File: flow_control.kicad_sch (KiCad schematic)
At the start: 64 parts, among them J10 Pump 1, J11 Temperature, J12 Pump 2, J13 Pump 3, J3 Flow, J7 Valve 1, J8 Valve 2, J9 Valve 3, Q1 MMBT3904, Q10 AO3401A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

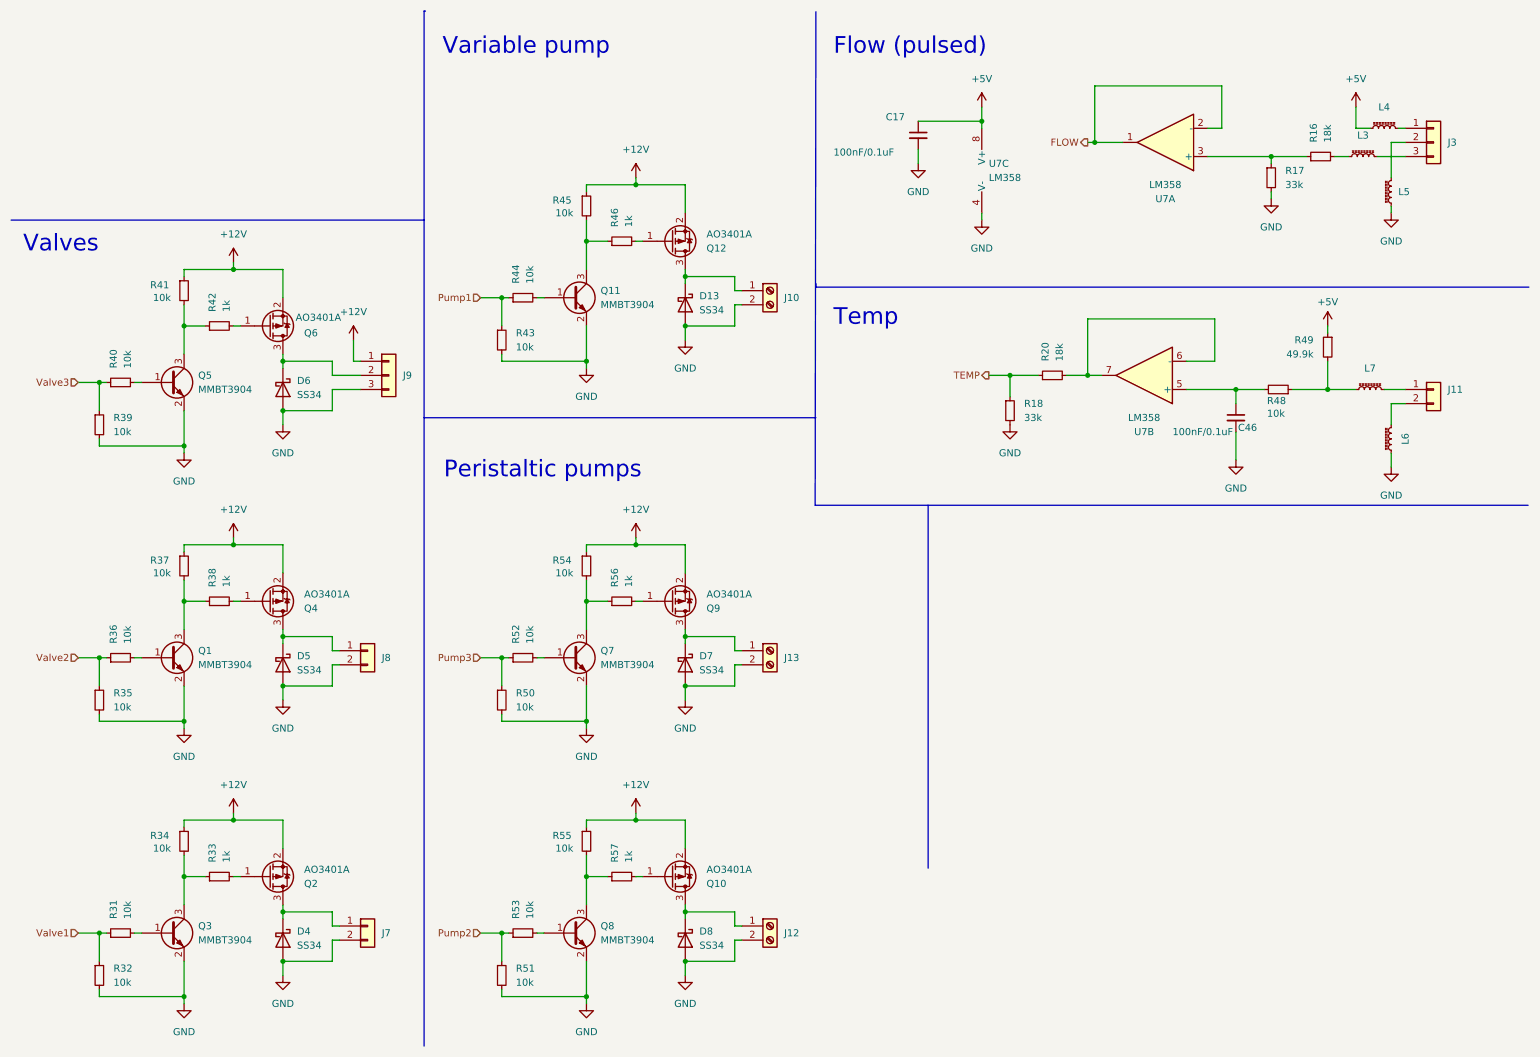
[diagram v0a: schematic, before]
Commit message: Replace 4 of the 6 highside outputs with TPS4H160B
See #50
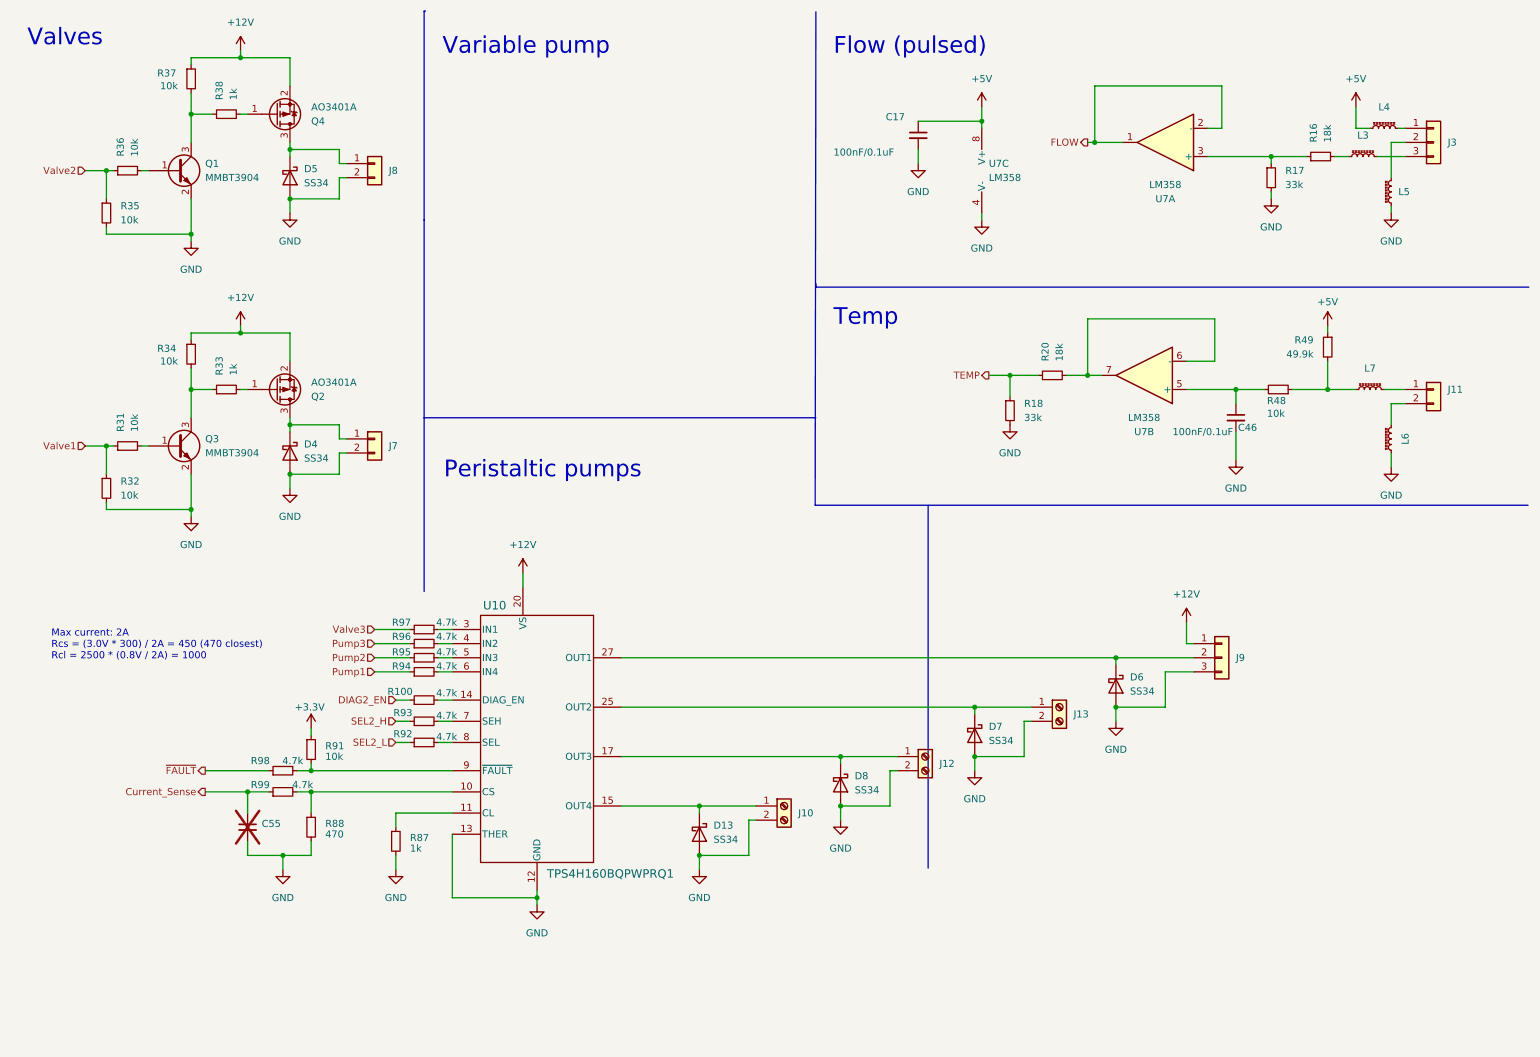
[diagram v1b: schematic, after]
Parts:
- removed Q10, Q12, Q6, Q9: AO3401A, Package_TO_SOT_SMD:SOT-23, symbol Transistor_FET:AO3401A
- removed Q11, Q5, Q7, Q8: MMBT3904, Package_TO_SOT_SMD:SOT-23, symbol Transistor_BJT:MMBT3904
- removed R39, R40, R41, R43, R44, R45, R50, R51, R52, R53, R54, R55: 10k, Resistor_SMD:R_0603_1608Metric, symbol Device:R_Small
- removed R42, R46, R56, R57: 1k, Resistor_SMD:R_0603_1608Metric, symbol Device:R_Small
- added C55: ~, Capacitor_SMD:C_0402_1005Metric, symbol Device:C_Small
- added R100, R92, R93, R94, R95, R96, R97, R98, R99: 4.7k, Resistor_SMD:R_0402_1005Metric, symbol Device:R_Small
- added R87: 1k, Resistor_SMD:R_0402_1005Metric, symbol Device:R_Small
- added R88: 470, Resistor_SMD:R_0402_1005Metric, symbol Device:R_Small
- added R91: 10k, Resistor_SMD:R_0402_1005Metric, symbol Device:R_Small
- added U10: TPS4H160BQPWPRQ1, Package_SO:HTSSOP-28-1EP_4.4x9.7mm_P0.65mm_EP2.85x5.4mm_ThermalVias, symbol HydroponicFlowerControl:TPS4H160BQPWPRQ1
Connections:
- net +12V: now also U10.20 (VS), U10.21 (VS), U10.22 (VS), U10.23 (VS)
- net GND: now also C55.2, R87.2, R88.2, U10.1 (GND), U10.12 (GND), U10.13 (THER), U10.29 (PAD)
- net Pump1: now also R94.1
- net Pump2: now also R95.1
- net Pump3: now also R96.1
- net Valve3: now also R97.1
- net at D7.1 (K), J13.1 (Pin_1): now also U10.25 (OUT2), U10.26 (OUT2)
- net at D8.1 (K), J12.1 (Pin_1): now also U10.17 (OUT3), U10.18 (OUT3)
- net at D13.1 (K), J10.1 (Pin_1): now also U10.15 (OUT4), U10.16 (OUT4)
- net at D6.1 (K), J9.2 (Pin_2): now also U10.27 (OUT1), U10.28 (OUT1)
- new net: R92.2, U10.8 (SEL)
- new net: R88.1, R99.2, U10.10 (CS)
- new net: R87.1, U10.11 (CL)
- new net: R100.2, U10.14 (DIAG_EN)
- new net: R97.2, U10.3 (IN1)
- new net: R96.2, U10.4 (IN2)
- new net: R95.2, U10.5 (IN3)
- new net: R94.2, U10.6 (IN4)
- new net: R93.2, U10.7 (SEH)
- new net: R91.2, R98.2, U10.9 (~{FAULT})
- new net +3.3V: R91.1
- new net Current_Sense: C55.1, R99.1
- new net DIAG2_EN: R100.1
- new net SEL2_H: R93.1
- new net SEL2_L: R92.1
- new net ~{FAULT}: R98.1
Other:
- note added: "Max current: 2A Rcs = (3.0V * 300) / 2A = 450 (470 closest) Rcl = 2500 * (0.8V / 2A) = 1000"
- moved on the sheet: D13, D4, D5, D6, D7, D8, J10, J12, J13, J7, J8, J9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

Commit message: Replace the last 2 of the highside outputs with TPS4H160B
Closes #50
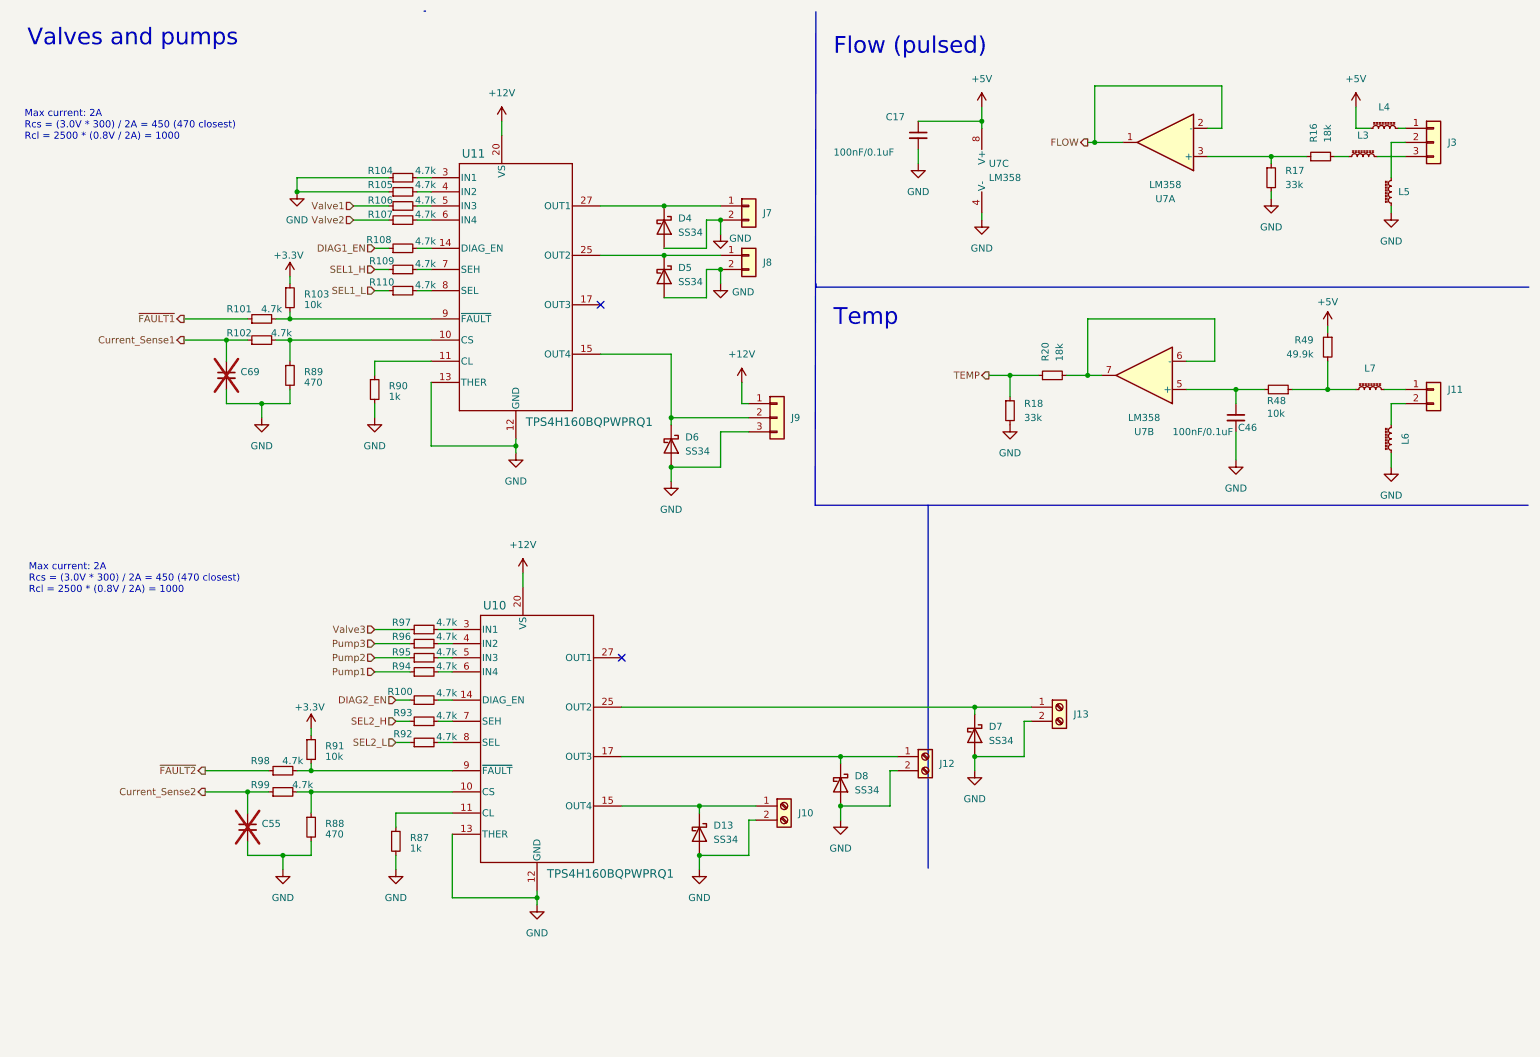
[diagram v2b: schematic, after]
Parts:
- removed Q1, Q3: MMBT3904, Package_TO_SOT_SMD:SOT-23, symbol Transistor_BJT:MMBT3904
- removed Q2, Q4: AO3401A, Package_TO_SOT_SMD:SOT-23, symbol Transistor_FET:AO3401A
- removed R31, R32, R34, R35, R36, R37: 10k, Resistor_SMD:R_0603_1608Metric, symbol Device:R_Small
- removed R33, R38: 1k, Resistor_SMD:R_0603_1608Metric, symbol Device:R_Small
- added C69: ~, Capacitor_SMD:C_0402_1005Metric, symbol Device:C_Small
- added R101, R102, R104, R105, R106, R107, R108, R109, R110: 4.7k, Resistor_SMD:R_0402_1005Metric, symbol Device:R_Small
- added R103: 10k, Resistor_SMD:R_0402_1005Metric, symbol Device:R_Small
- added R89: 470, Resistor_SMD:R_0402_1005Metric, symbol Device:R_Small
- added R90: 1k, Resistor_SMD:R_0402_1005Metric, symbol Device:R_Small
- added U11: TPS4H160BQPWPRQ1, Package_SO:HTSSOP-28-1EP_4.4x9.7mm_P0.65mm_EP2.85x5.4mm_ThermalVias, symbol HydroponicFlowerControl:TPS4H160BQPWPRQ1
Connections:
- net +12V: now also U11.20 (VS), U11.21 (VS), U11.22 (VS), U11.23 (VS)
- net +3.3V: now also R103.1
- net GND: now also C69.2, R104.1, R105.1, R89.2, R90.2, U11.1 (GND), U11.12 (GND), U11.13 (THER), U11.29 (PAD)
- net Valve1: now also R106.1
- net Valve2: now also R107.1
- net at D4.1 (K), J7.1 (Pin_1): now also U11.27 (OUT1), U11.28 (OUT1)
- net at D5.1 (K), J8.1 (Pin_1): now also U11.25 (OUT2), U11.26 (OUT2)
- net at D6.1 (K), J9.2 (Pin_2): now also U11.15 (OUT4), U11.16 (OUT4); no longer U10.27 (OUT1), U10.28 (OUT1)
- net Current_Sense renamed Current_Sense2
- net ~{FAULT} renamed ~{FAULT2}
- new net: R102.2, R89.1, U11.10 (CS)
- new net: R90.1, U11.11 (CL)
- new net: R108.2, U11.14 (DIAG_EN)
- new net: U11.17 (OUT3), U11.18 (OUT3)
- new net: R104.2, U11.3 (IN1)
- new net: R105.2, U11.4 (IN2)
- new net: R106.2, U11.5 (IN3)
- new net: R107.2, U11.6 (IN4)
- new net: R109.2, U11.7 (SEH)
- new net: R110.2, U11.8 (SEL)
- new net: R101.2, R103.2, U11.9 (~{FAULT})
- new net: U10.27 (OUT1), U10.28 (OUT1)
- new net Current_Sense1: C69.1, R102.1
- new net DIAG1_EN: R108.1
- new net SEL1_H: R109.1
- new net SEL1_L: R110.1
- new net ~{FAULT1}: R101.1
- no-connect marks 0 -> 2
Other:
- note added: "Valves and pumps"
- note removed: "Peristaltic pumps"
- note removed: "Valves"
- note removed: "Variable pump"
- moved on the sheet: D4, D5, D6, J7, J8, J9

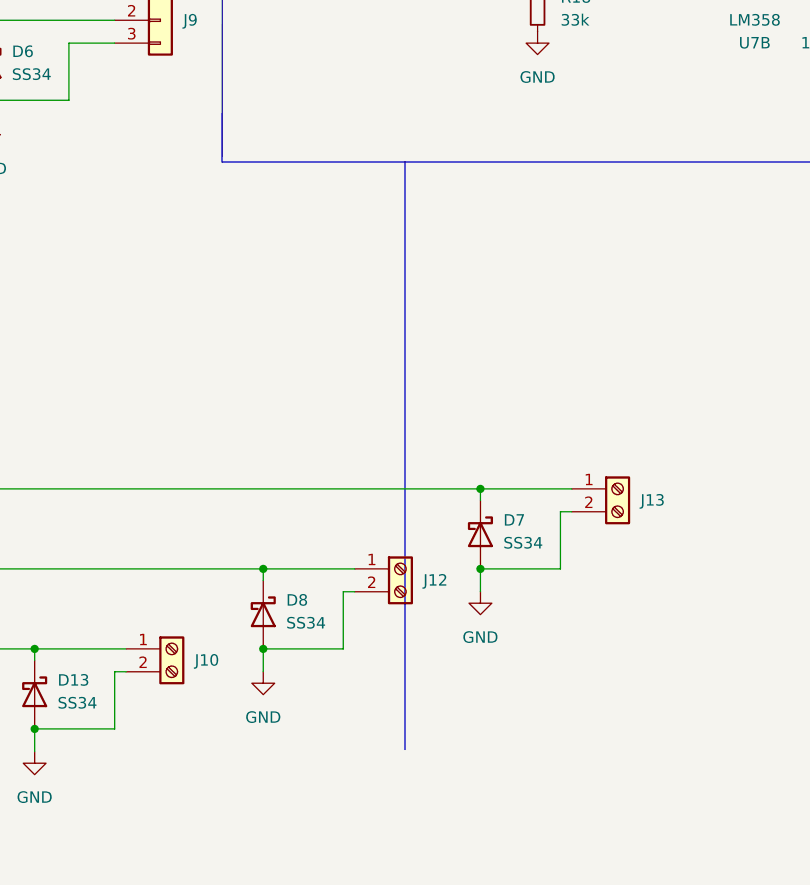
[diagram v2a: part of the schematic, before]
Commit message: Add ADC for input voltage
Closes #59
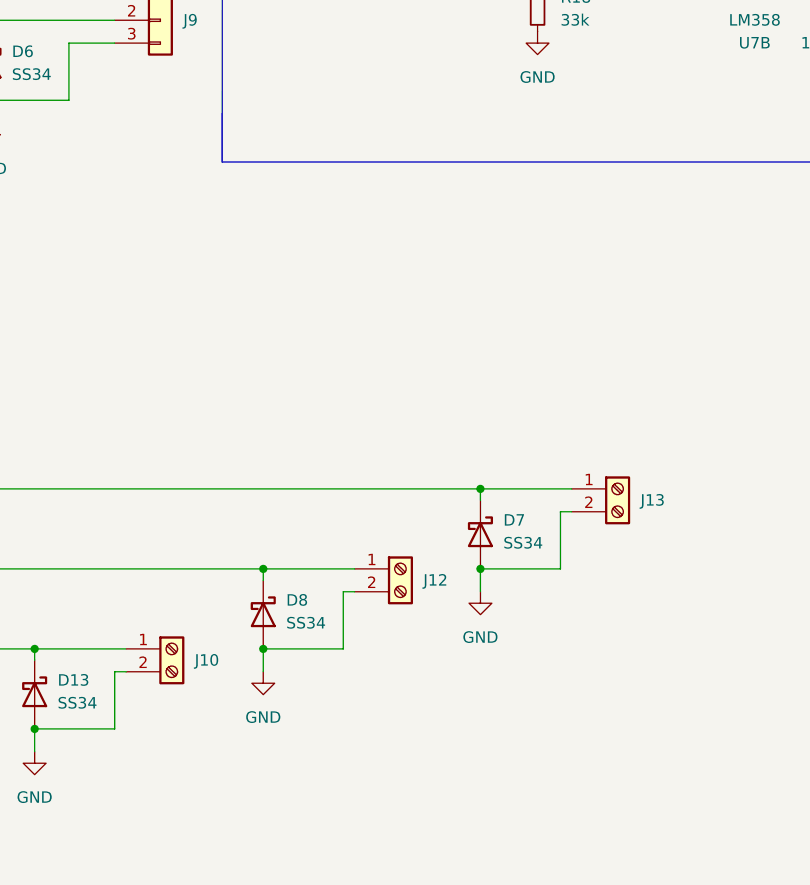
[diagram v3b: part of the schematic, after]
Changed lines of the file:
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@@
-		)
-	)
-	(polyline
-		(pts
-			(xy 177.038 100.838) (xy 177.038 166.116)
-		)
-		(stroke
-			(width 0)
-			(type default)
 		)
 	)

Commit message: Update files to KiCad 10.0
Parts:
- C55, C69: value ~ -> (none); now in the parts list

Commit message: Fix mismatch between inputs to highside switches and outputs
Closes #60
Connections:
- net GND: now also R106.1, R97.1; no longer R104.1, R105.1
- net Valve1: now also R104.1; no longer R106.1
- net Valve2: now also R105.1; no longer R107.1
- net Valve3: now also R107.1; no longer R97.1
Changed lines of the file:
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@@
 	)
 	(junction
-		(at 63.5 44.45)
-		(diameter 0)
-		(color 0 0 0 0)
-	)
-	(junction
 		(at 185.42 146.05)
 		(diameter 0)
@@
 	(wire
 		(pts
+			(xy 73.66 44.45) (xy 80.01 44.45)
+		)
+		(stroke
+			(width 0)
+			(type default)
+		)
+	)
+	(wire
+		(pts
 			(xy 139.7 58.42) (xy 139.7 60.96)
 		)
@@
 	(wire
 		(pts
-			(xy 63.5 41.91) (xy 80.01 41.91)
-		)
-		(stroke
-			(width 0)
-			(type default)
-		)
-	)
-	(wire
-		(pts
 			(xy 46.99 152.4) (xy 54.61 152.4)
 		)
@@
 		)
 	)
+	(wire
+		(pts
+			(xy 63.5 46.99) (xy 63.5 49.53)
+		)
+		(stroke
+			(width 0)
+			(type default)
+		)
+	)
 	(polyline
 		(pts
@@
 	(wire
 		(pts
+			(xy 66.04 123.19) (xy 83.82 123.19)
+		)
+		(stroke
+			(width 0)
+			(type default)
+		)
+	)
+	(wire
+		(pts
+			(xy 73.66 41.91) (xy 80.01 41.91)
+		)
+		(stroke
+			(width 0)
+			(type default)
+		)
+	)
+	(wire
+		(pts
 			(xy 81.28 156.21) (xy 81.28 158.75)
 		)
@@
 	(wire
 		(pts
+			(xy 66.04 123.19) (xy 66.04 124.46)
+		)
+		(stroke
+			(width 0)
+			(type default)
+		)
+	)
+	(wire
+		(pts
 			(xy 261.62 33.02) (xy 262.89 33.02)
 		)
@@
 	(wire
 		(pts
-			(xy 73.66 46.99) (xy 80.01 46.99)
-		)
-		(stroke
-			(width 0)
-			(type default)
-		)
-	)
-	(wire
-		(pts
 			(xy 194.31 146.05) (xy 185.42 146.05)
 		)
@@
 	(wire
 		(pts
+			(xy 63.5 46.99) (xy 80.01 46.99)
+		)
+		(stroke
+			(width 0)
+			(type default)
+		)
+	)
+	(wire
+		(pts
 			(xy 63.5 148.59) (xy 66.04 148.59)
 		)
@@
 	(wire
 		(pts
-			(xy 77.47 123.19) (xy 83.82 123.19)
-		)
-		(stroke
-			(width 0)
-			(type default)
-		)
-	)
-	(wire
-		(pts
 			(xy 46.99 148.59) (xy 58.42 148.59)
 		)
@@
 	(wire
 		(pts
-			(xy 63.5 44.45) (xy 80.01 44.45)
-		)
-		(stroke
-			(width 0)
-			(type default)
-		)
-	)
-	(wire
-		(pts
 			(xy 57.15 82.55) (xy 57.15 85.09)
 		)
@@
 	(wire
 		(pts
-			(xy 63.5 41.91) (xy 63.5 44.45)
-		)
-		(stroke
-			(width 0)
-			(type default)
-		)
-	)
-	(wire
-		(pts
 			(xy 207.01 35.56) (xy 212.09 35.56)
 		)
@@
 	(hierarchical_label "Valve2"
 		(shape input)
-		(at 73.66 49.53 180)
+		(at 73.66 44.45 180)
 		(effects
 			(font
@@
 	(hierarchical_label "Valve3"
 		(shape input)
-		(at 77.47 123.19 180)
+		(at 73.66 49.53 180)
 		(effects
 			(font
@@
 	(hierarchical_label "Valve1"
 		(shape input)
-		(at 73.66 46.99 180)
+		(at 73.66 41.91 180)
 		(effects
 			(font
@@
 	)
 	(symbol
+		(lib_id "power:GND")
+		(at 66.04 124.46 0)
+		(unit 1)
+		(body_style 1)
+		(exclude_from_sim no)
+		(in_bom yes)
+		(on_board yes)
+		(in_pos_files yes)
+		(dnp no)
+		(fields_autoplaced yes)
+		(property "Reference" "#PWR0128"
+			(at 66.04 130.81 0)
+			(hide yes)
+			(show_name no)
+			(do_not_autoplace no)
+			(effects
+				(font
+					(size 1.27 1.27)
+				)
+			)
+		)
+		(property "Value" "GND"
+			(at 66.04 129.54 0)
+			(show_name no)
+			(do_not_autoplace no)
+			(effects
+				(font
+					(size 1.27 1.27)
+				)
+			)
+		)
+		(property "Footprint" ""
+			(at 66.04 124.46 0)
+			(hide yes)
+			(show_name no)
+			(do_not_autoplace no)
+			(effects
+				(font
+					(size 1.27 1.27)
+				)
+			)
+		)
+		(property "Datasheet" ""
+			(at 66.04 124.46 0)
+			(hide yes)
+			(show_name no)
+			(do_not_autoplace no)
+			(effects
+				(font
+					(size 1.27 1.27)
+				)
+			)
+		)
+		(property "Description" "Power symbol creates a global label with name \"GND\" , ground"
+			(at 66.04 124.46 0)
+			(hide yes)
+			(show_name no)
+			(do_not_autoplace no)
+			(effects
+				(font
+					(size 1.27 1.27)
+				)
+			)
+		)
+		(pin "1"
+		)
+		(instances
+			(project "HydroponicFlowerControl"
+				(path "/b3c8a28b-9ce1-4002-b8e8-ef8cb73fe031/7c7300e5-25d5-4b1e-a176-ffcbce070bf3"
+					(reference "#PWR0128")
+					(unit 1)
+				)
+			)
+		)
+	)
+	(symbol
 		(lib_id "Diode:SS34")
 		(at 185.42 142.24 270)
@@
 	(symbol
 		(lib_id "power:GND")
-		(at 63.5 44.45 0)
+		(at 63.5 49.53 0)
 		(unit 1)
 		(body_style 1)
@@
 		(fields_autoplaced yes)
 		(property "Reference" "#PWR0107"
-			(at 63.5 50.8 0)
+			(at 63.5 55.88 0)
 			(hide yes)
 			(show_name no)
@@
 		)
 		(property "Value" "GND"
-			(at 63.5 49.53 0)
+			(at 63.5 54.61 0)
 			(show_name no)
 			(do_not_autoplace no)
@@
 		)
 		(property "Footprint" ""
-			(at 63.5 44.45 0)
+			(at 63.5 49.53 0)
 			(hide yes)
 			(show_name no)
@@
 		)
 		(property "Datasheet" ""
-			(at 63.5 44.45 0)
+			(at 63.5 49.53 0)
 			(hide yes)
 			(show_name no)
@@
 		)
 		(property "Description" "Power symbol creates a global label with name \"GND\" , ground"
-			(at 63.5 44.45 0)
+			(at 63.5 49.53 0)
 			(hide yes)
 			(show_name no)
